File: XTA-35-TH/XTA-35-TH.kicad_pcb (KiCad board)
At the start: 4 copper layers, 100 x 98.7 mm, 30 parts, among them J1 XTA_Connector, J2 XTA Power, J3 LED, J4 SD0, J5 SD1, J6 DEBUG, SW1 Boot Override, SW2 Reset, U1 74LVC245, U2 74LVC245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

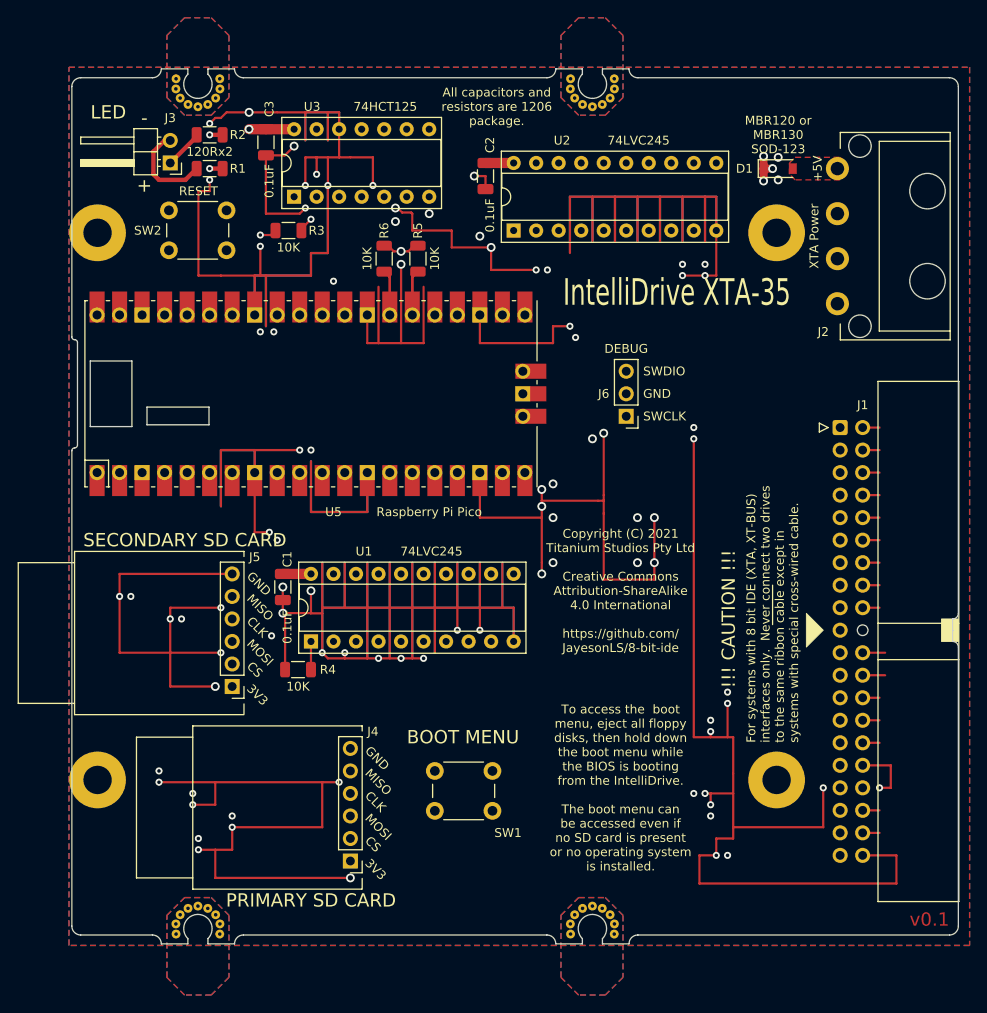
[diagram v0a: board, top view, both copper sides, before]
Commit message: Start of alternate layout which better locates the SD cards. Also adds cutouts for side-screw clearance.
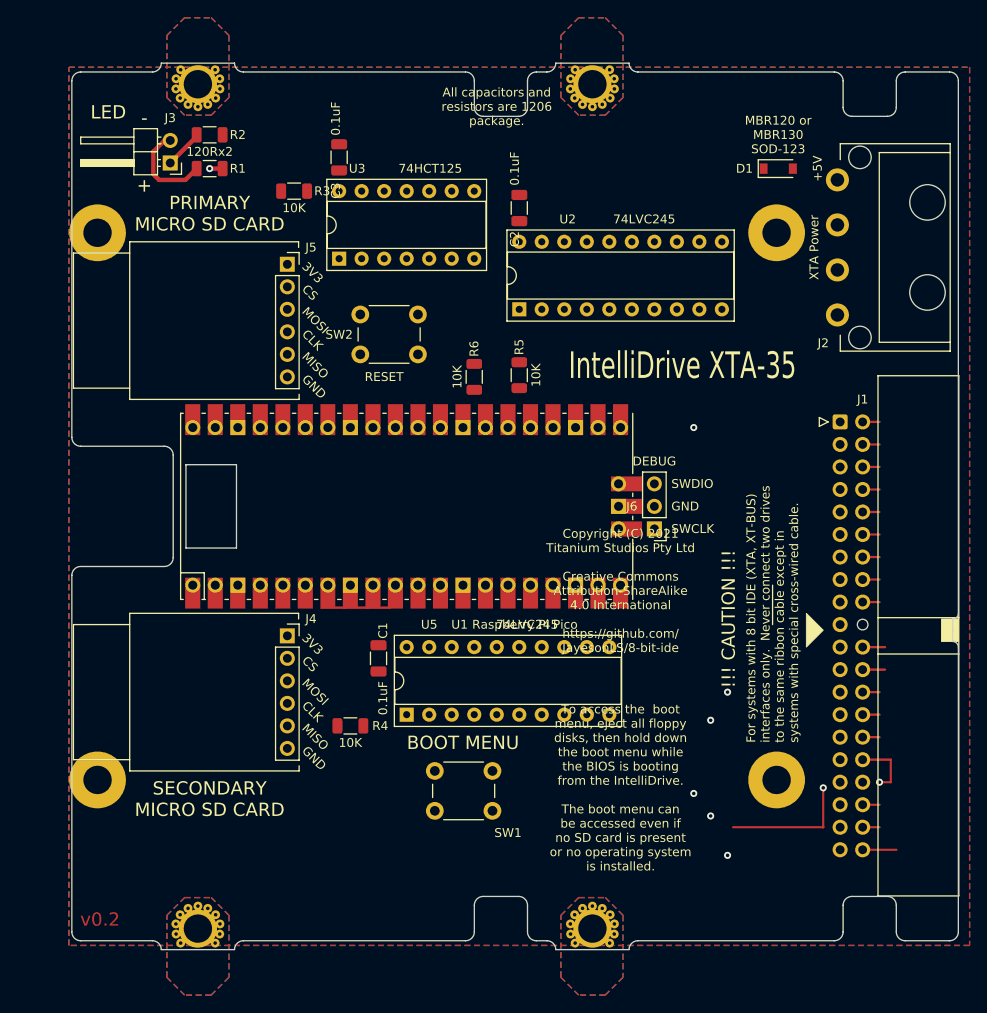
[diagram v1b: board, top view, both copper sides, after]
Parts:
- J4, J5: footprint 00Common:SD_Board -> 00Common:SD_Board_SD_Socket_Down
- moved J5 48.0 mm to (174.6, 52.7), turned to 0 degrees
- moved J4 26.3 mm to (174.6, 94.6), turned to 0 degrees
- moved SW2 24.6 mm to (189.2, 62.9)
- moved R5 17.4 mm to (200.7, 65.2)
- moved R6 16.8 mm to (195.6, 65.4)
- moved U5 16.7 mm to (188.0, 80.0)
- moved U1 13.6 mm to (188.0, 103.5)
- moved C1 13.5 mm to (184.8, 97.2)
- moved J6 13.1 mm to (215.9, 82.5)
- moved U2 8.91 mm to (200.7, 57.8)
- moved R4 8.67 mm to (181.6, 104.8)
- moved U3 8.64 mm to (180.3, 52.1)
- moved C3 8.43 mm to (180.3, 40.6), turned to 90 degrees
- moved C2 5.25 mm to (200.7, 46.4), turned to 90 degrees
- moved R3 4.49 mm to (175.3, 44.5)
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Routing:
- net GND: track 973.8 -> 64.8 mm, vias 58 -> 2
- net +3V3: track 183.2 -> 0.00 mm, vias 10 -> 0
- net /~BOOT_OVERRIDE: track 86.9 -> 0.00 mm, vias 2 -> 0
- net SPI_RX: track 70.2 -> 0.00 mm, vias 2 -> 0
- net D0: track 69.3 -> 0.00 mm
- net D1: track 66.7 -> 0.00 mm
- net D2: track 64.2 -> 0.00 mm
- net DRQ: track 112.6 -> 48.4 mm, vias 1 -> 0
- net VSYS: track 63.5 -> 0.00 mm, vias 6 -> 0
- net SD0_CS: track 62.1 -> 0.00 mm, vias 1 -> 0
- net SPI_SCK: track 61.0 -> 0.00 mm, vias 2 -> 0
- net D3: track 60.9 -> 0.00 mm
- net SPI_TX: track 58.6 -> 1.47 mm, vias 1 -> 0
- net IRQ: track 103.8 -> 51.0 mm, vias 1 -> 0
- net D4: track 52.4 -> 0.00 mm
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- removed copper zone on In1.Cu, net +3V3
- removed copper zone on In2.Cu, net +3V3
- removed copper zone on F.Cu, net /5V_IN
- removed copper zone on In1.Cu, net VSYS
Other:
- board size 100 x 98.7 mm -> 100 x 100 mm
- board text added: "PRIMARY MICRO SD CARD"
- board text added: "SECONDARY MICRO SD CARD"
- board text added: "v0.2"
- board text removed: "PRIMARY SD CARD"
- board text removed: "SECONDARY SD CARD"
- board text removed: "v0.1"
